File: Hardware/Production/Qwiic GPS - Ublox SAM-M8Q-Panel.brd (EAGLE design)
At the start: 101.9 x 101.9 mm, 283 parts, among them J10 PTH, J14 PTH, J3 PTH, J6 PTH, U1 SAM-M8Q, U2 SAM-M8Q, U3 SAM-M8Q, U4 SAM-M8Q

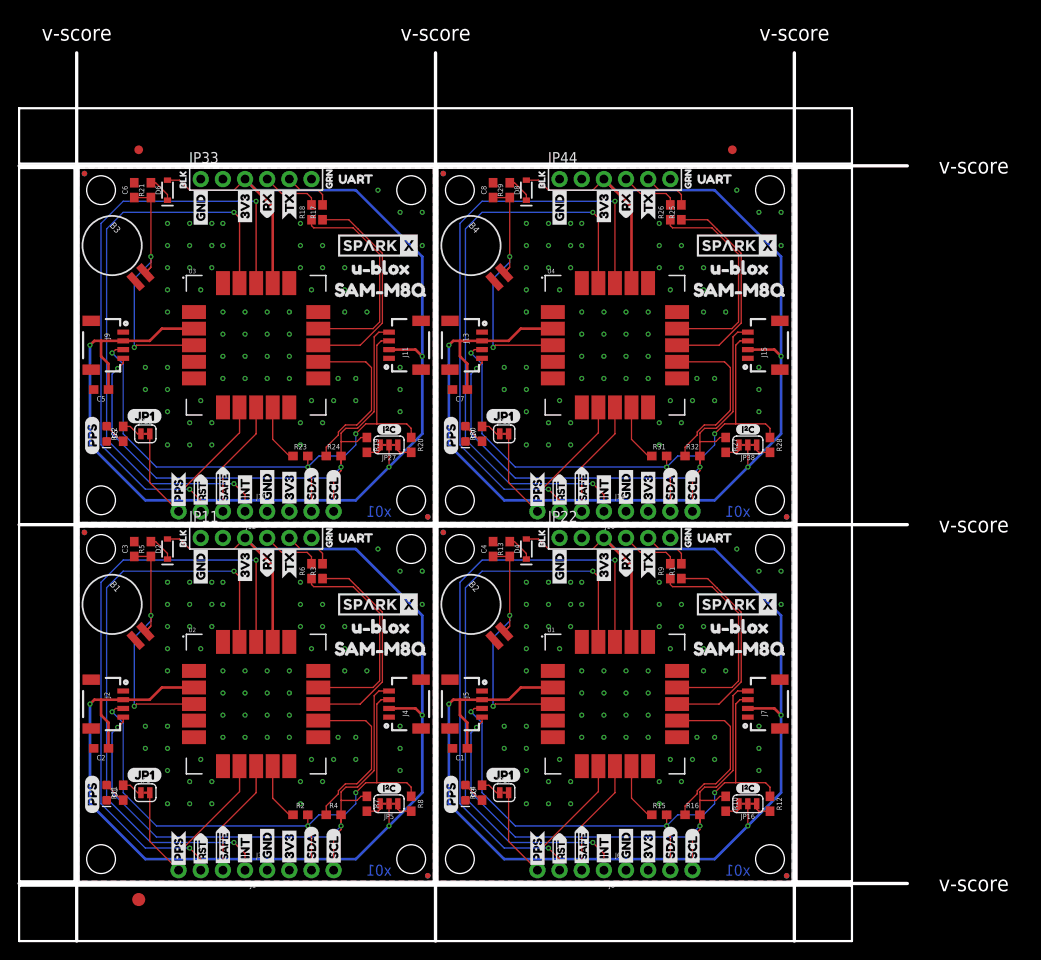
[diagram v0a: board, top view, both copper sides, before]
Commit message: Removing single unit files. Removing notes from schematic.
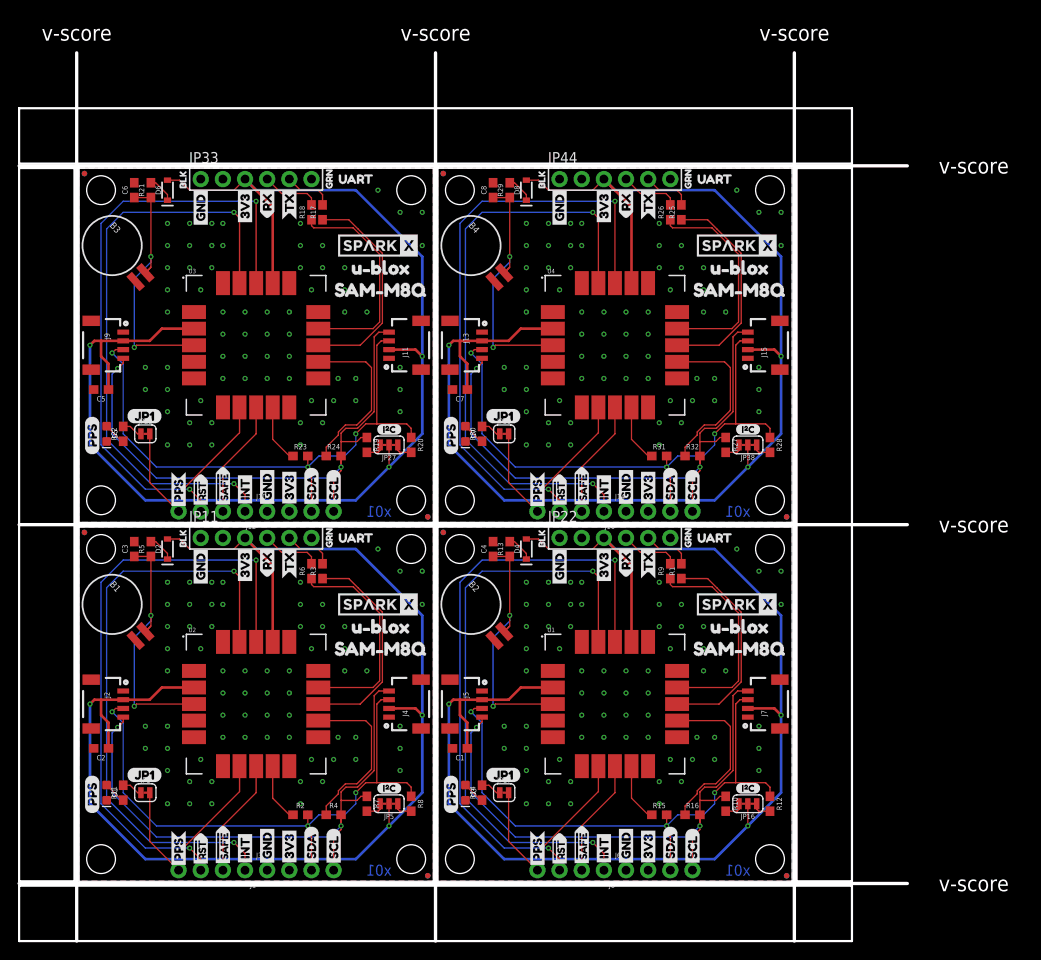
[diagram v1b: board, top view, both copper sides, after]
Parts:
- removed E$1, E$2: (no value), SparkFun-Aesthetics:FIDUCIAL-1X2
- removed E$3: (no value), SparkFun-Retired:FIDUCIAL-1.5X3
- D1, D3, D5, D7: value BLUE -> Yellow
- JP1, JP17, JP28, JP39: value JUMPER-SMT_2_NC_TRACE_SILK -> (none)
- R11, R14, R22, R30: value 470 -> 1k

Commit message: Updated battery footprint
Footprint for the battery is now for the reflowable version
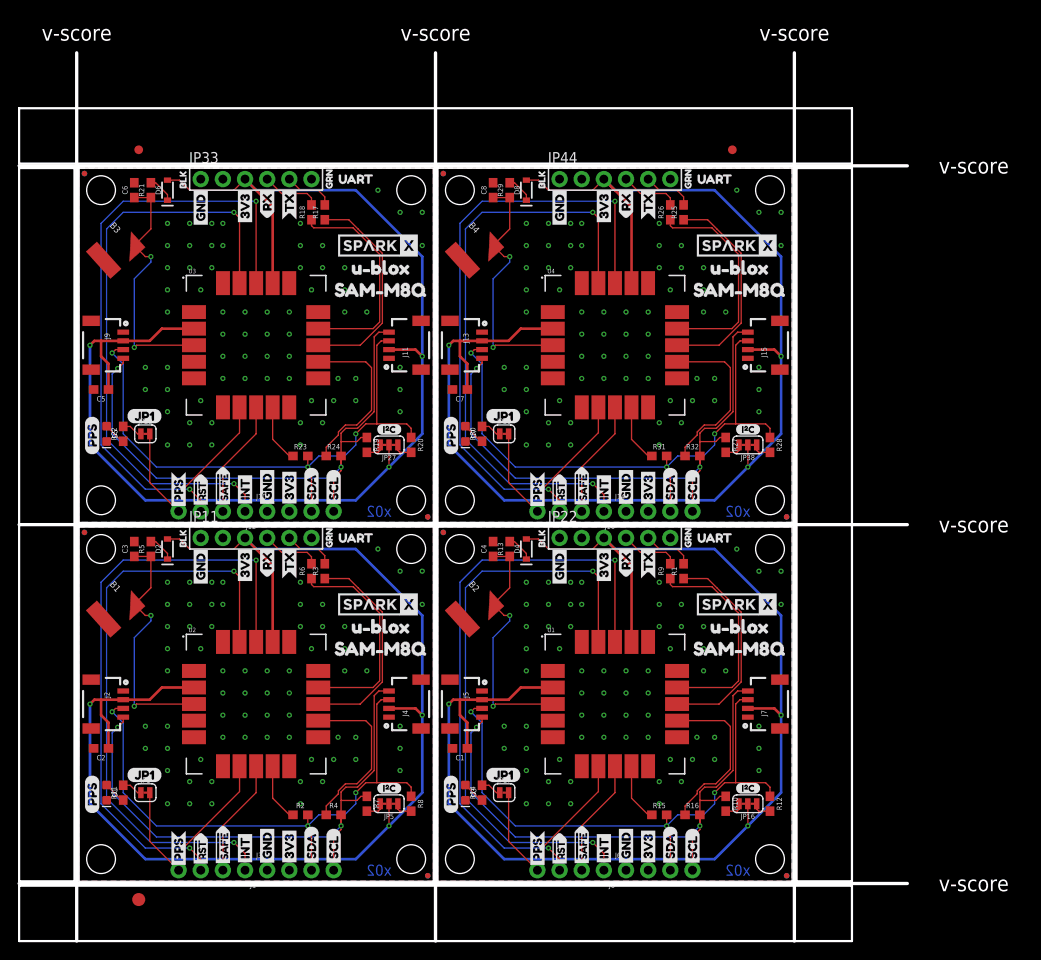
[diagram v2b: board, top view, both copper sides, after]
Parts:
- added E$1, E$2: (no value), SparkFun-Aesthetics:FIDUCIAL-1X2
- added E$3: (no value), SparkFun-Retired:FIDUCIAL-1.5X3
- B1, B2, B3, B4: device SparkFun-Batteries:BATTCON-6.8MM -> SparkFun-Batteries:ML414H_IV01E
- U$101, U$141, U$61: value (none) -> SPARKX-LOGO4; device Labels:QWIIC-LOGO-MEDIUM -> SparkX:SPARKX-MEDIUM
- U$103, U$143, U$63: value SPARKX-LOGO4 -> (none); device SparkX:SPARKX-MEDIUM -> Labels:3V3-04
- U$105, U$145, U$65: device Labels:3V3-04 -> Labels:GND-04
- U$107, U$147, U$67: device Labels:GND-04 -> buzzard_labels (7):#RST3
- U$109, U$149, U$69: device buzzard_labels (7):#RST3 -> buzzard_labels (7):#SAFE1
- U$111, U$151, U$71: device buzzard_labels (7):#SAFE1 -> buzzard_labels (7):PPS5
- U$113, U$153, U$73: device buzzard_labels (7):PPS5 -> buzzard_labels (7):UART0
- U$115, U$155, U$75: device buzzard_labels (7):UART0 -> buzzard_labels (8):BLK1
- U$117, U$157, U$77: device buzzard_labels (8):BLK1 -> buzzard_labels (8):GRN2
- U$119, U$159, U$79: device buzzard_labels (8):GRN2 -> buzzard_labels (8):JP10
- U$120, U$160, U$80: device buzzard_labels (8):JP10 -> Labels:QWIIC-LOGO-LARGE
- U$28: device Labels:SDA-[) -> Labels:QWIIC-LOGO-LARGE
- U$30: device Labels:QWIIC-LOGO-MEDIUM -> Labels:SDA-[)
- moved U$113 41.8 mm to (28.8, 80.5), flipped to the top, turned to 0 degrees
- moved U$153 41.8 mm to (70.0, 80.5), flipped to the top, turned to 0 degrees
- moved U$73 41.8 mm to (70.0, 39.4), flipped to the top, turned to 0 degrees
- moved U$119 34.4 mm to (5.46, 53.3), flipped to the top, turned to 0 degrees
- moved U$159 34.4 mm to (46.6, 53.3), flipped to the top, turned to 0 degrees
- moved U$79 34.4 mm to (46.6, 12.2), flipped to the top, turned to 0 degrees
- moved U$28 33.1 mm to (35.6, 8.89), flipped to the bottom, turned to 0 degrees
- moved U$30 33.1 mm to (67.8, 1.65), flipped to the top, turned to 90 degrees
- moved U$67 32.3 mm to (55.1, 1.40), flipped to the top
- moved U$107 32.3 mm to (14.0, 42.5), flipped to the top
- moved U$147 32.3 mm to (55.1, 42.5), flipped to the top
- moved U$120 30.3 mm to (35.6, 50.0), flipped to the bottom
- moved U$160 30.3 mm to (76.7, 50.0), flipped to the bottom
- moved U$80 30.3 mm to (76.7, 8.89), flipped to the bottom
- moved U$101 22.9 mm to (34.3, 72.9), flipped to the top
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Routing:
- net BACKUP: track 29.8 -> 28.5 mm
- net BACKUP1: track 29.8 -> 28.5 mm
- net BACKUP3: track 29.8 -> 28.5 mm
- net BACKUP2: track 29.8 -> 28.5 mm
- net 3.3V1: track 150.2 -> 149.4 mm
- net 3.3V: track 150.2 -> 149.4 mm
- net 3.3V3: track 150.2 -> 149.4 mm
- net 3.3V2: track 150.2 -> 149.4 mm
- net SDA3: track 68.0 -> 67.5 mm
- net SDA2: track 68.0 -> 67.5 mm
- net SDA1: track 68.0 -> 67.5 mm
- net SDA: track 68.0 -> 67.5 mm
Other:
- board text added: "x02"
- board text removed: "x01"
